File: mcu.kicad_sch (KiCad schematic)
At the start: 24 parts

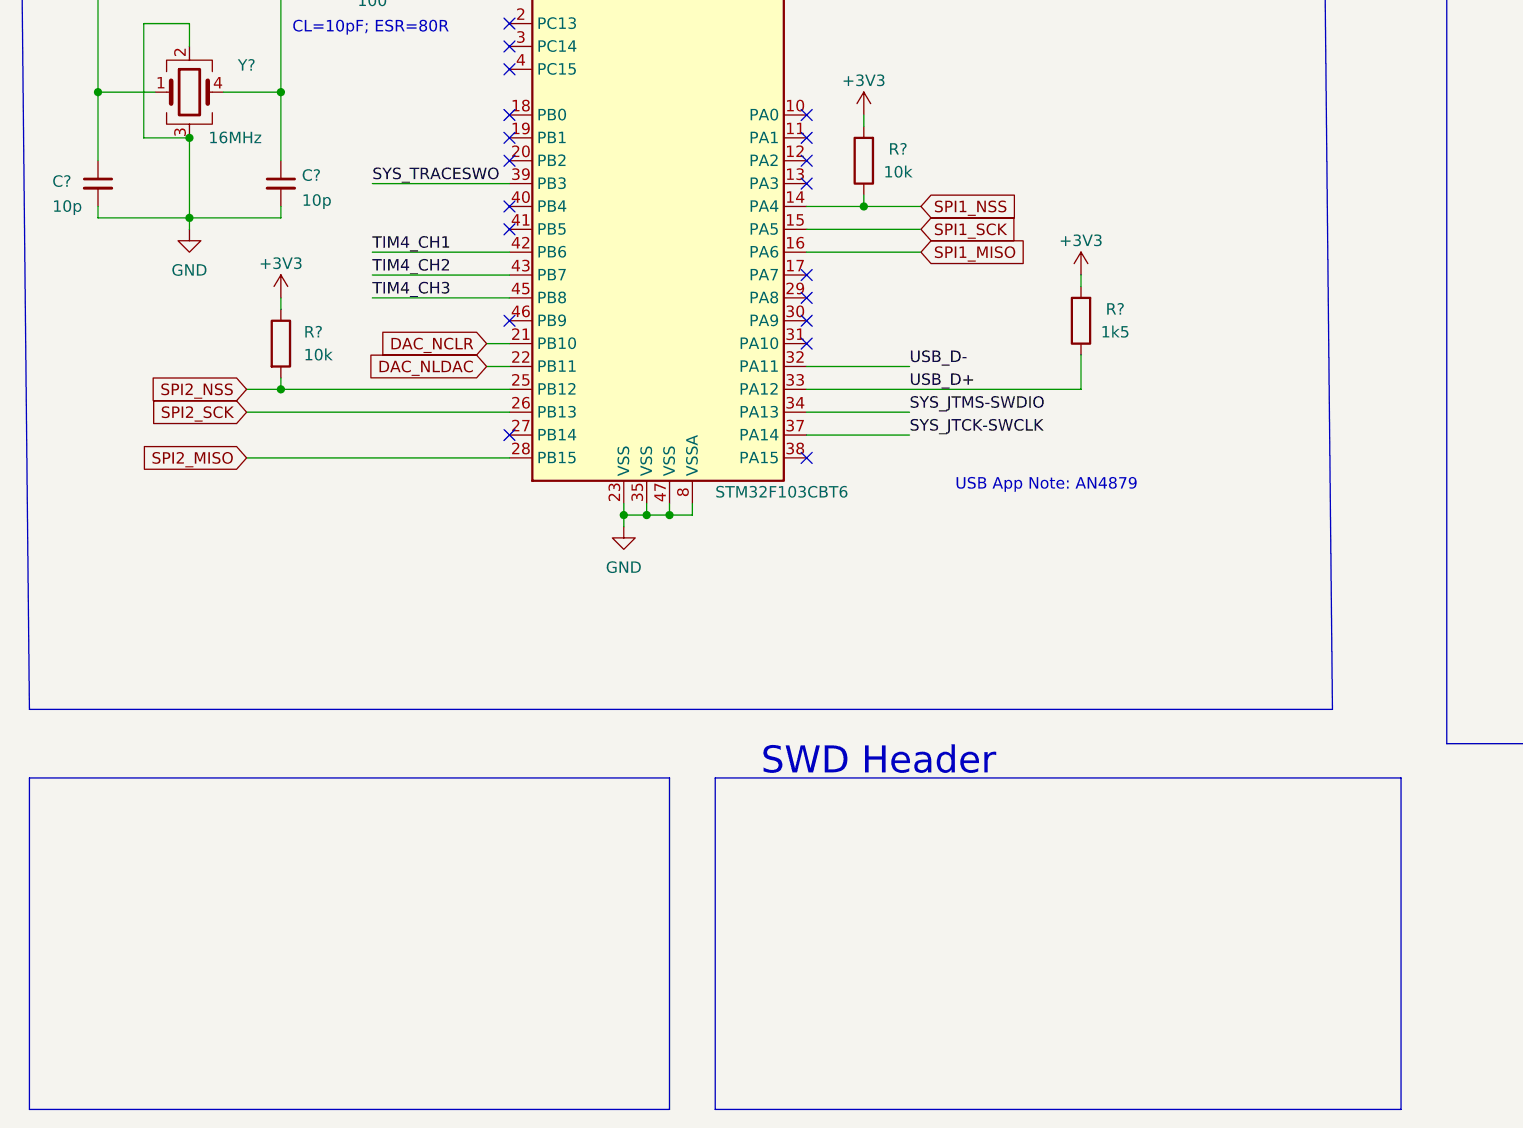
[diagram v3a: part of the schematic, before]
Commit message: Completed SWD header and RGB LED schematic
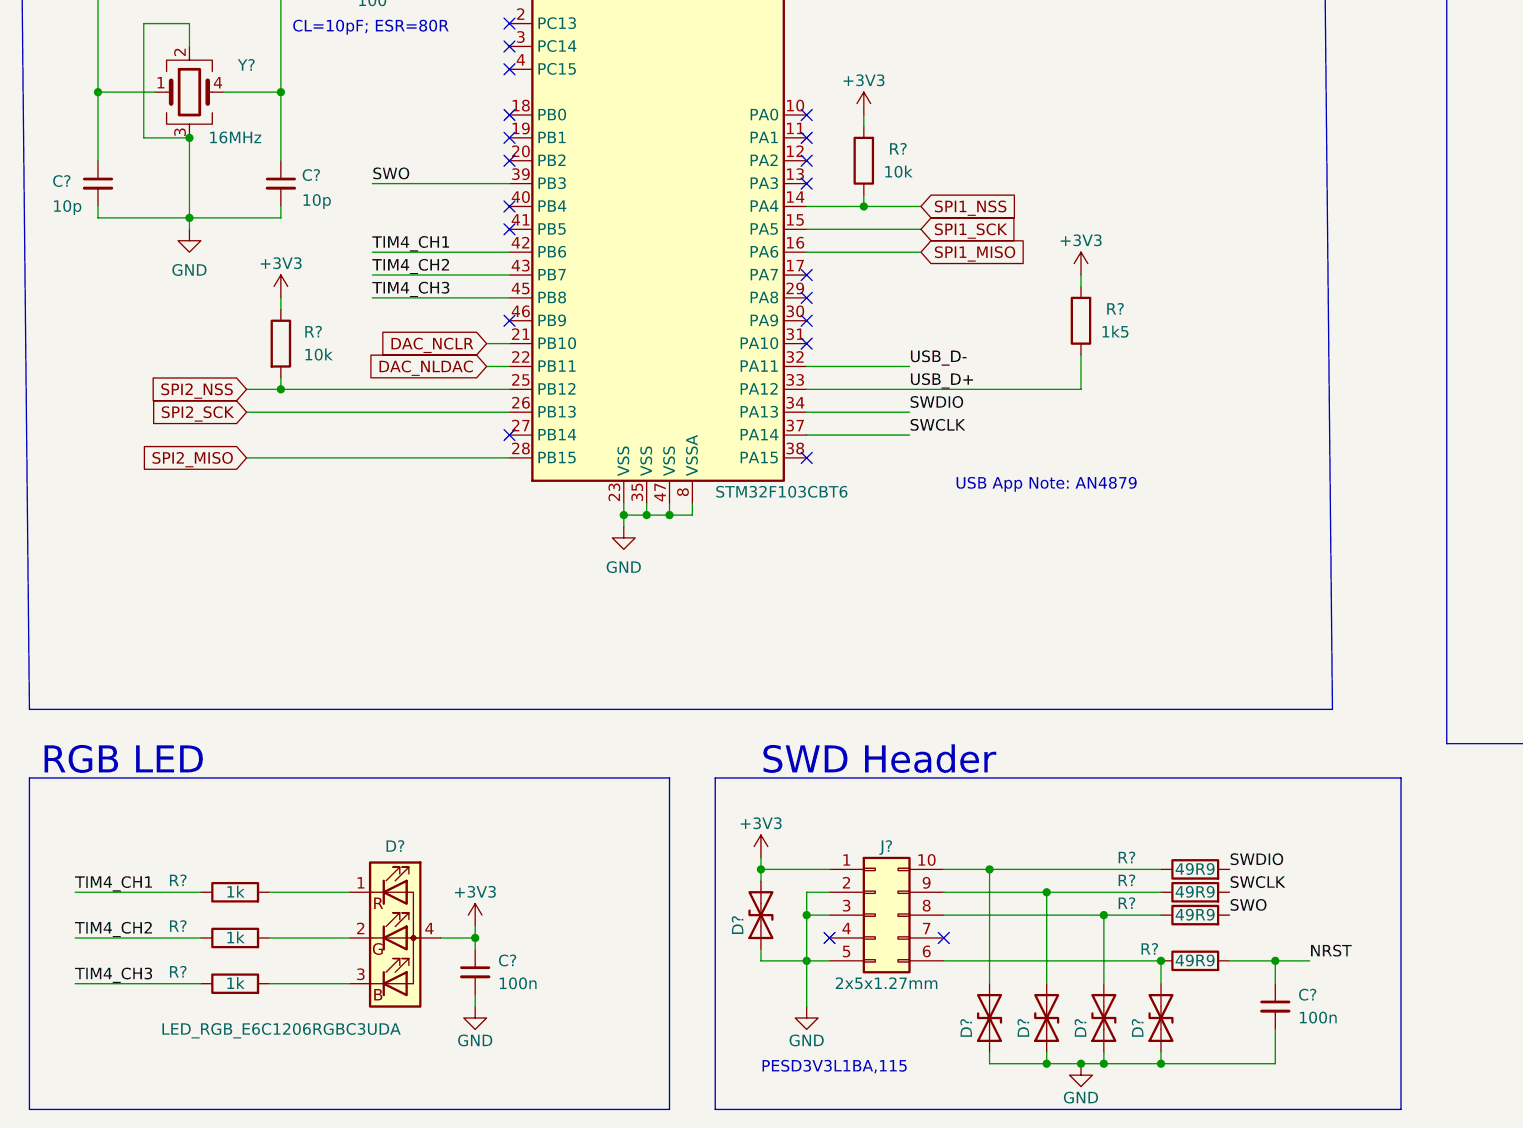
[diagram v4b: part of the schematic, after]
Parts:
- added C? (x2): 100n, symbol Device:C_Small
- added D? (x5): D_TVS, symbol Device:D_TVS
- added D?: LED_RGB_E6C1206RGBC3UDA, symbol Device:LED_RGBA
- added J?: 2x5x1.27mm, symbol Connector_Generic:Conn_02x05_Counter_Clockwise
- added R? (x4): 49R9, symbol Device:R
- added R? (x3): 1k, symbol Device:R
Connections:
- net +3V3: now also C?.1, D?.2 (A2), D?.4 (A), J?.1 (Pin_1)
- net GND: now also C?.2, C?.2, D?.1 (A1), D?.1 (A1), D?.1 (A1), D?.1 (A1), D?.1 (A1), J?.2 (Pin_2), J?.3 (Pin_3), J?.5 (Pin_5)
- net NRST: now also C?.1, R?.2
- net TIM4_CH1: now also R?.1
- net TIM4_CH2: now also R?.1
- net TIM4_CH3: now also R?.1
- net SYS_JTCK-SWCLK renamed SWCLK
- net SWCLK: now also R?.2
- net SYS_JTMS-SWDIO renamed SWDIO
- net SWDIO: now also R?.2
- net SYS_TRACESWO renamed SWO
- net SWO: now also R?.2
- new net: D?.2 (A2), J?.6 (Pin_6), R?.1
- new net: D?.3 (BK), R?.2
- new net: D?.2 (A2), J?.8 (Pin_8), R?.1
- new net: D?.2 (A2), J?.10 (Pin_10), R?.1
- new net: D?.2 (A2), J?.9 (Pin_9), R?.1
- new net: D?.2 (GK), R?.2
- new net: D?.1 (RK), R?.2
- no-connect marks 22 -> 24
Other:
- note added: "PESD3V3L1BA,115"
- note added: "RGB LED"

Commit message: ERC valid.
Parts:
- gave numbers to parts that had none: 40

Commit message: Assigned Footprints and Set up board specifications.
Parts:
- C200, C206, C207: footprint (none) -> Capacitor_SMD:C_0603_1608Metric
- C201, C202, C203, C204, C205, C208, C209, C210, C211, C212: footprint (none) -> Capacitor_SMD:C_0402_1005Metric
- D200, D202, D203, D204, D205: footprint (none) -> Diode_SMD:D_SOD-323
- D201: footprint (none) -> LED_SMD:LED_Cree-PLCC4_2x2mm_CW
- J200: footprint (none) -> Connector_USB:USB_C_Receptacle_HRO_TYPE-C-31-M-12
- J201: footprint (none) -> Connector_PinHeader_1.27mm:PinHeader_2x05_P1.27mm_Vertical_SMD
- L200: footprint (none) -> Inductor_SMD:L_0402_1005Metric
- R200, R201, R202, R203, R204, R205, R206, R207, R208, R209, R210, R211, R212, R213: footprint (none) -> Resistor_SMD:R_0402_1005Metric
- Y200: footprint (none) -> Crystal:Crystal_SMD_3225-4Pin_3.2x2.5mm
